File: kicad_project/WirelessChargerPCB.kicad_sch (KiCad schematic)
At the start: 26 parts, among them J1 Screw_Terminal_01x02, J2 Screw_Terminal_01x02, Q1 BD139, Q2 IRFZ44NS, U1 NE555D

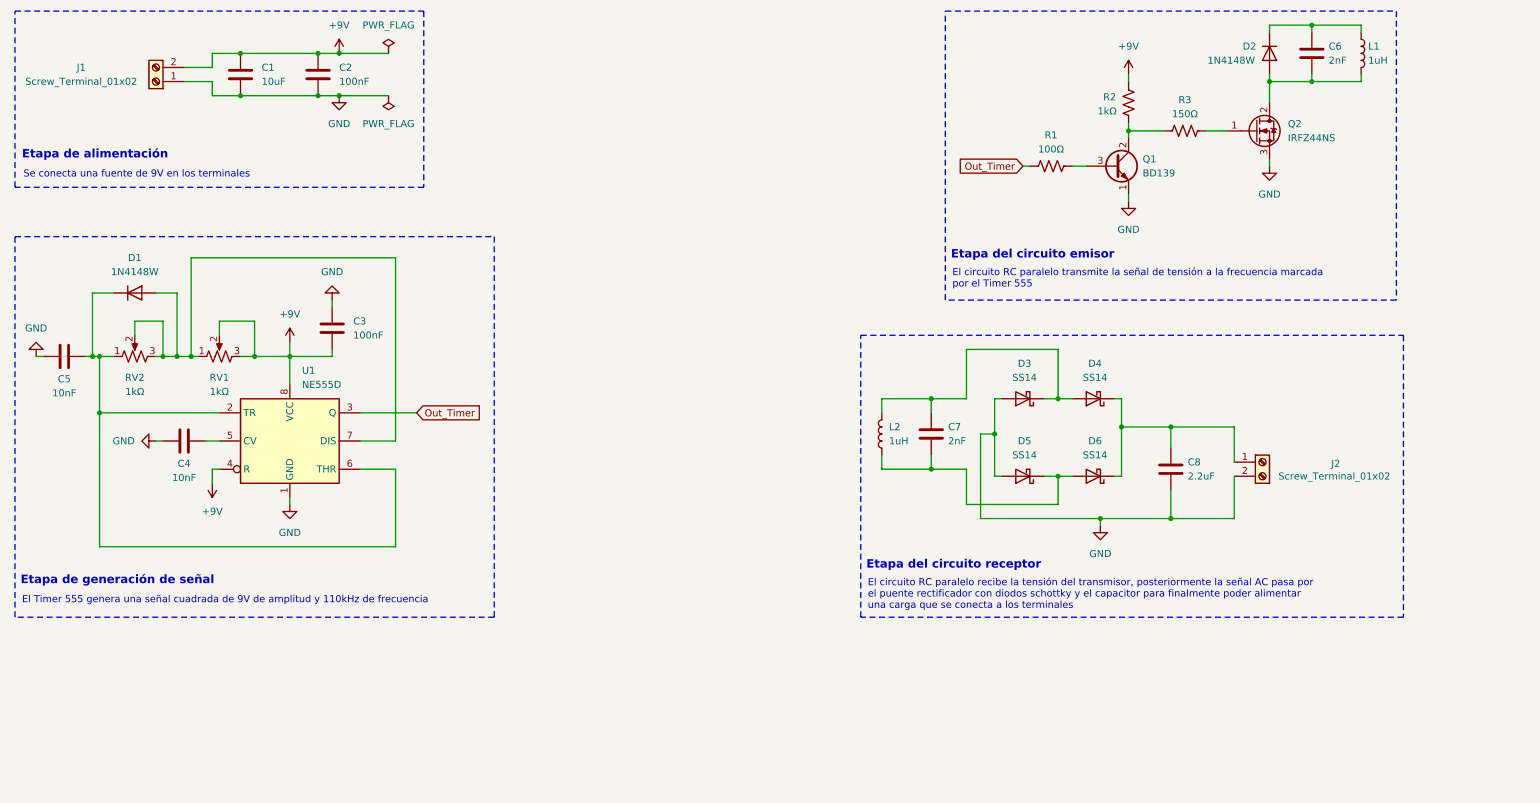
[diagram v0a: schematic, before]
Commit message: Agregando huellas y modelos 3D, además de otros cambios en el editor de placas y esquemático
Signed-off-by: ant0305 <anthonycalvo50@gmail.com>
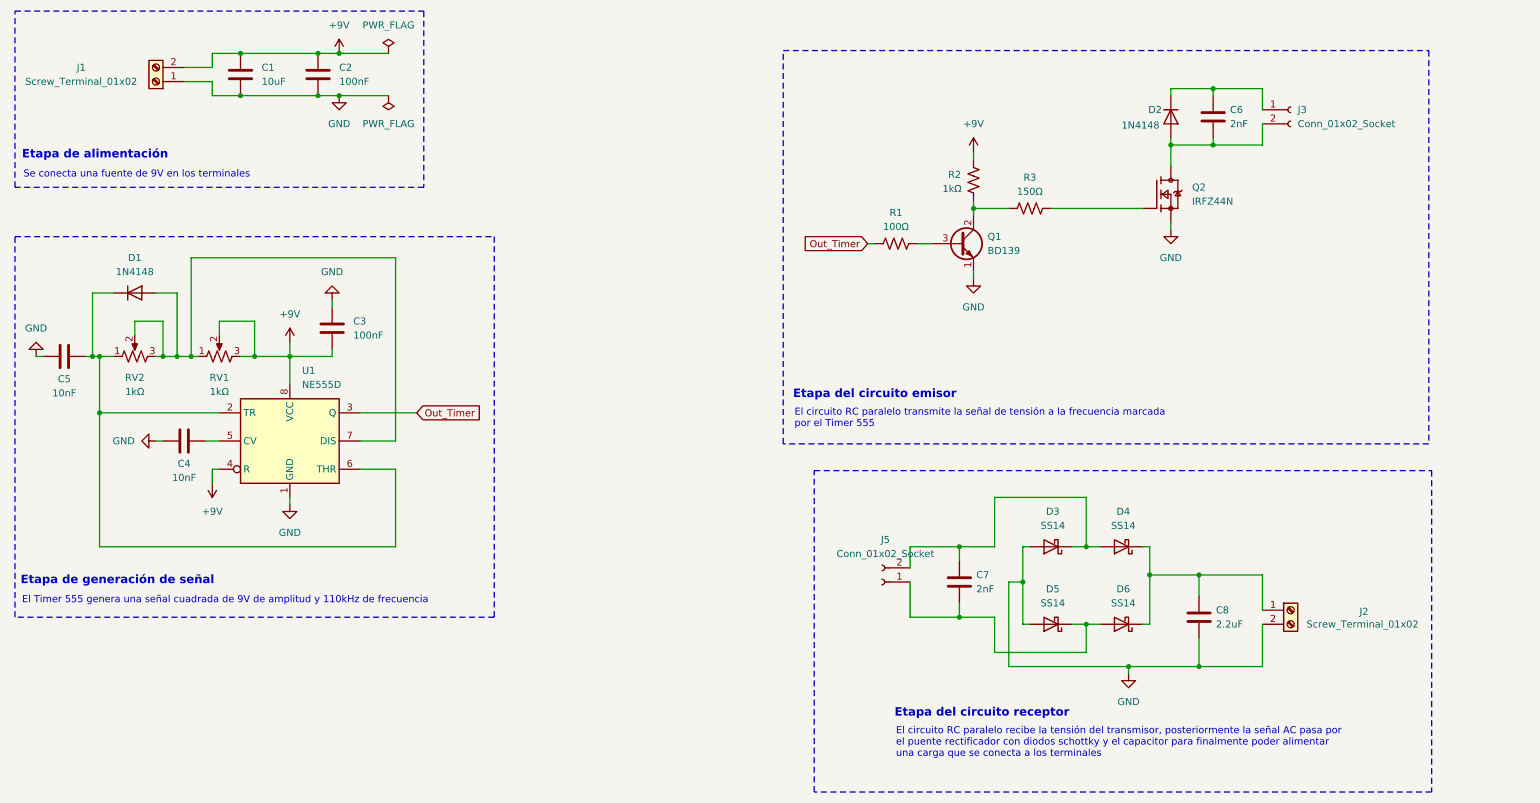
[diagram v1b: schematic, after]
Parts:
- removed D1, D2: 1N4148W, Diode_SMD:D_SOD-123, symbol Diode:1N4148W
- removed L1, L2: 1uH, symbol Device:L
- removed Q2: IRFZ44NS, Package_TO_SOT_SMD:TO-263-2, symbol Device:Q_NMOS_GDS
- added D1, D2: 1N4148, Diode_THT:D_DO-35_SOD27_P7.62mm_Horizontal, symbol Diode:1N4148
- added J3, J5: Conn_01x02_Socket, Connector_PinSocket_2.54mm:PinSocket_1x02_P2.54mm_Vertical, symbol Connector:Conn_01x02_Socket
- added Q2: IRFZ44N, Huellas:TO254P1016X419X2286-3, symbol IRFZ44N:IRFZ44N
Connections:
- net GND: now also Q2.3
- net at RV1.1, RV2.2, RV2.3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: now also D1.2 (A)
- net at C6.1: now also D2.1 (K), J3.1 (Pin_1)
- net at C6.2: now also D2.2 (A), J3.2 (Pin_2), Q2.2
- net at R3.2: now also Q2.1
- net at C5.2, RV2.1, U1.2 (TR)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: now also D1.1 (K)
- net at C7.1, D3.1 (K), D4.2 (A): now also J5.2 (Pin_2)
- net at C7.2, D5.1 (K), D6.2 (A): now also J5.1 (Pin_1)
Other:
- moved on the sheet: C6, C7, C8, D3, D4, D5, D6, J2, Q1, R1, R2, R3

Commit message: Agregando huellas de Heatsinks y relizando acomodo de ambas PCBs
Signed-off-by: RoMadrigal <rmadrigalmontes@gmail.com>
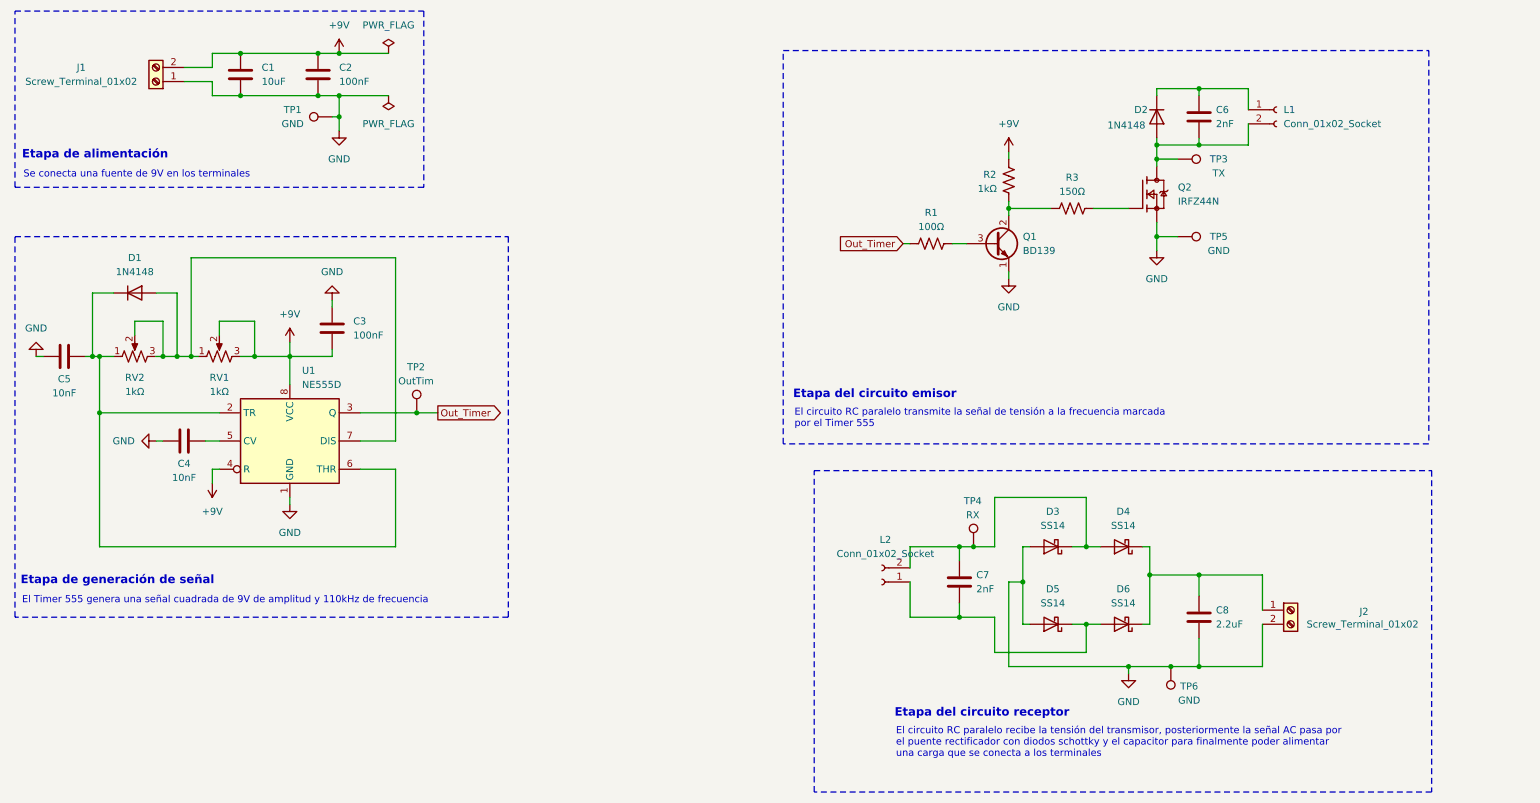
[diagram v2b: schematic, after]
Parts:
- added TP1, TP5, TP6: GND, Connector_PinHeader_2.54mm:PinHeader_1x01_P2.54mm_Vertical, symbol Connector:TestPoint
- added TP2: OutTim, Connector_PinHeader_2.54mm:PinHeader_1x01_P2.54mm_Vertical, symbol Connector:TestPoint
- added TP3: TX, Connector_PinHeader_2.54mm:PinHeader_1x01_P2.54mm_Vertical, symbol Connector:TestPoint
- added TP4: RX, Connector_PinHeader_2.54mm:PinHeader_1x01_P2.54mm_Vertical, symbol Connector:TestPoint
- renumbered J3 to L1, J5 to L2
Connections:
- net GND: now also TP1.1, TP5.1, TP6.1
- net Out_Timer: now also TP2.1
- net at C6.2, D2.2 (A), L1.2 (Pin_2)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: now also TP3.1
- net at C7.1, D3.1 (K), D4.2 (A)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: now also TP4.1
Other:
- moved on the sheet: C6, D2, L1, Q1, Q2, R1, R2, R3

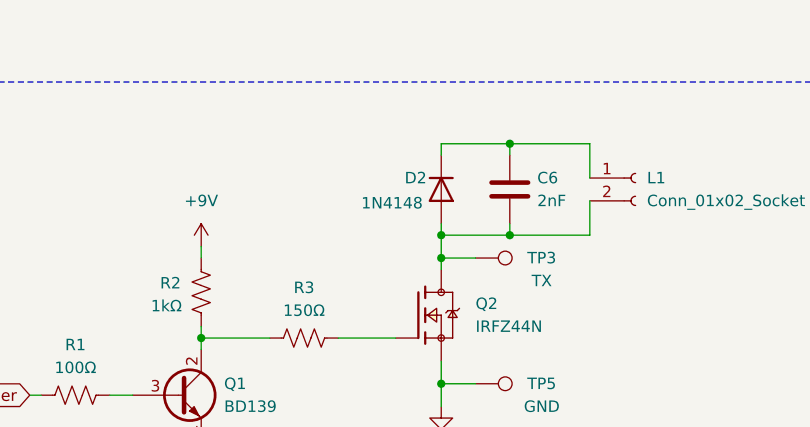
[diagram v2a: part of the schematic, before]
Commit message: Agregando una conexion faltante en el esquematico y actualizando el editor de placas
Signed-off-by: ant0305 <anthonycalvo50@gmail.com>
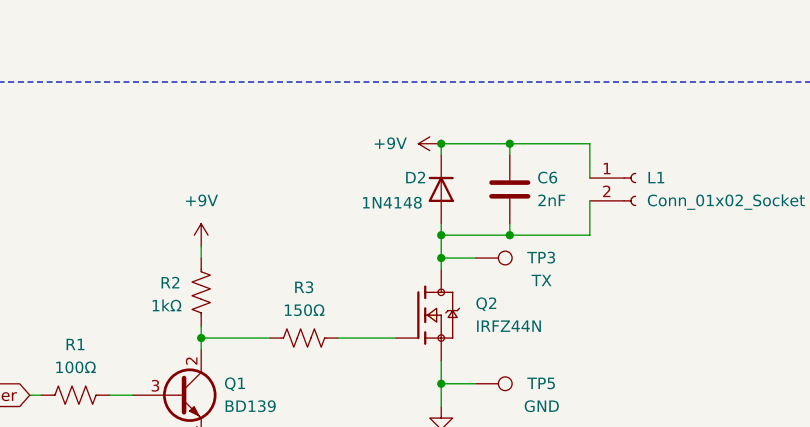
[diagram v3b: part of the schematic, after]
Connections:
- net +9V: now also C6.1, D2.1 (K), L1.1 (Pin_1)
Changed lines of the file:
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@@
+	)
+	(junction
+		(at 231.14 35.56)
+		(diameter 0)
+		(color 0 0 0 0)
 	)
 	(junction
@@
 					(unit 1)
 				)
+			)
+		)
+	)
+	(symbol
+		(lib_id "power:+9V")
+		(at 231.14 35.56 90)
+		(unit 1)
+		(exclude_from_sim no)
+		(in_bom yes)
+		(on_board yes)
+		(dnp no)
+		(fields_autoplaced yes)
+		(property "Reference" "#PWR013"
+			(at 234.95 35.56 0)
+			(effects
+				(font
+					(size 1.27 1.27)
+				)
+				(hide yes)
+			)
+		)
+		(property "Value" "+9V"
+			(at 227.33 35.5599 90)
+			(effects
+				(font
+					(size 1.27 1.27)
+				)
+				(justify left)
+			)
+		)
+		(property "Footprint" ""
+			(at 231.14 35.56 0)
+			(effects
+				(font
+					(size 1.27 1.27)
+				)
+				(hide yes)
+			)
+		)
+		(property "Datasheet" ""
+			(at 231.14 35.56 0)
+			(effects
+				(font
+					(size 1.27 1.27)
+				)
+				(hide yes)
+			)
+		)
+		(property "Description" "Power symbol creates a global label with name \"+9V\""
+			(at 231.14 35.56 0)
+			(effects
+				(font
+					(size 1.27 1.27)
+				)
+				(hide yes)
+			)
+		)
+		(pin "1"
+		)
+		(instances
+			(project "WirelessChargerPCB"
+				(path "/b69418bb-1d9c-4542-932d-c618456e07de"
+					(reference "#PWR013")
+					(unit 1)
+				)

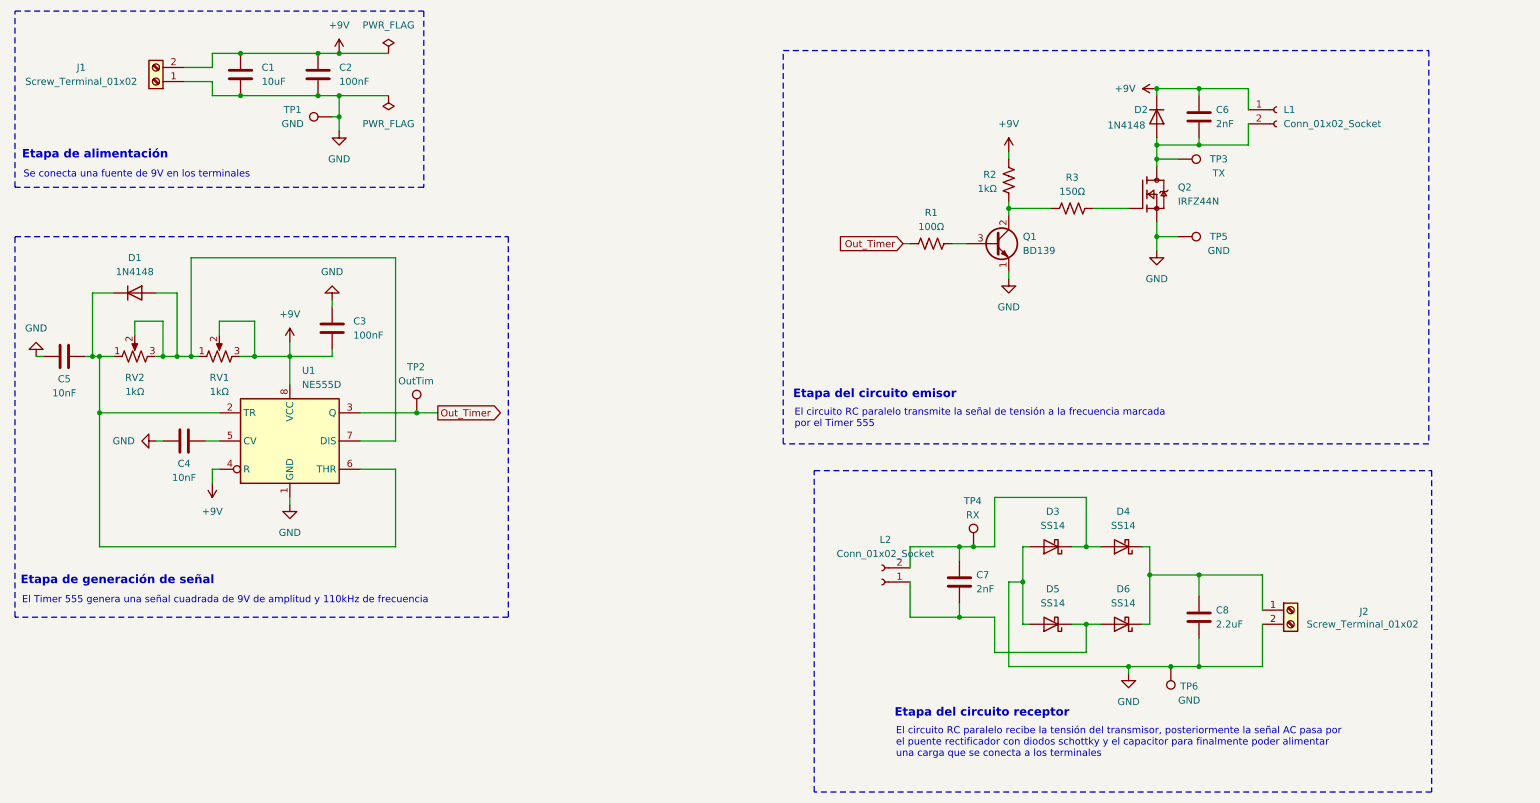
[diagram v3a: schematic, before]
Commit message: Agregando nuevos puntos de prueba y corrigiendo +9V faltante
Signed-off-by: RoMadrigal <rmadrigalmontes@gmail.com>
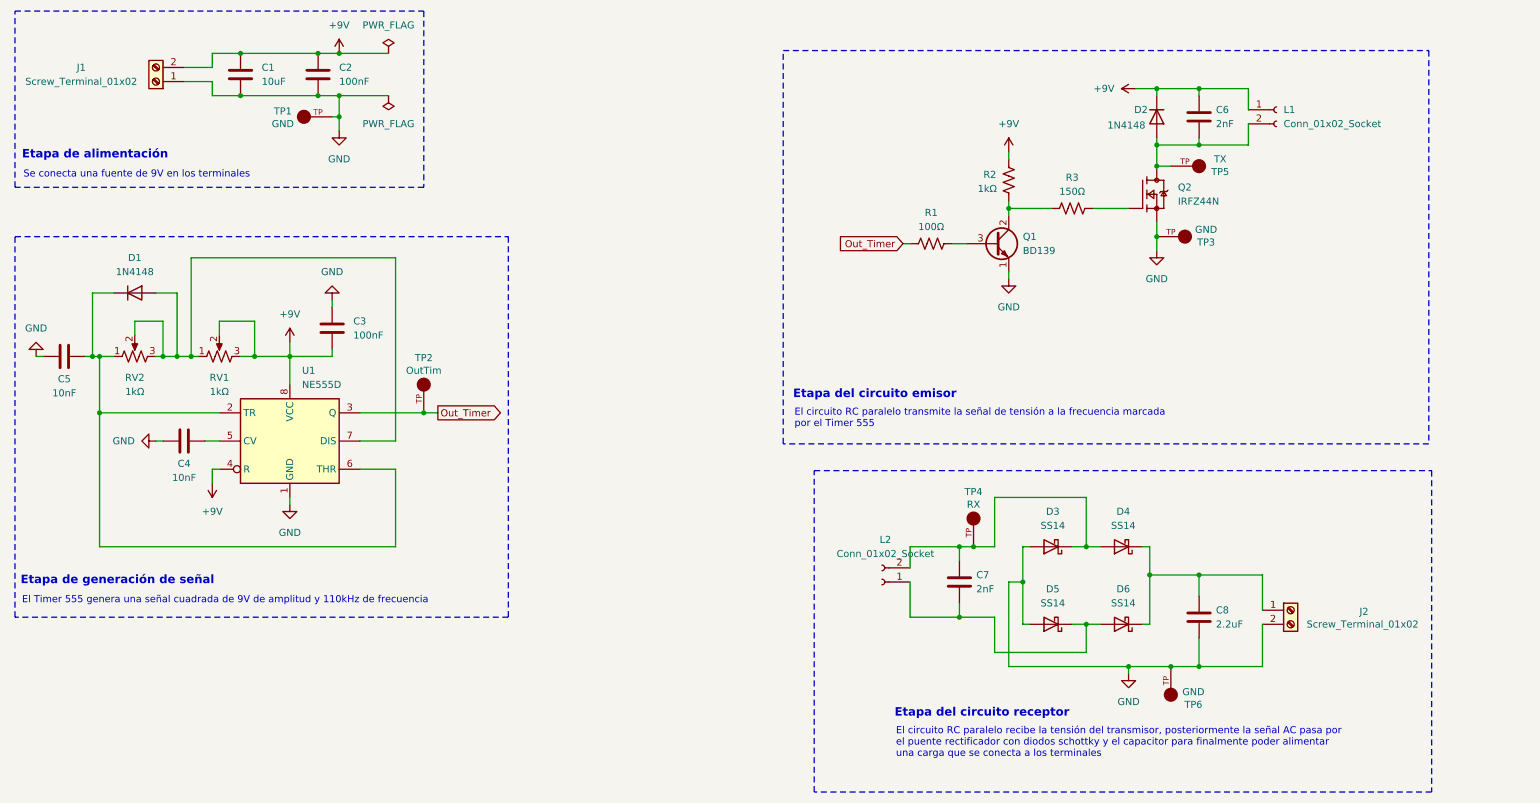
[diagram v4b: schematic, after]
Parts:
- removed TP1, TP5, TP6: GND, Connector_PinHeader_2.54mm:PinHeader_1x01_P2.54mm_Vertical, symbol Connector:TestPoint
- removed TP2: OutTim, Connector_PinHeader_2.54mm:PinHeader_1x01_P2.54mm_Vertical, symbol Connector:TestPoint
- removed TP3: TX, Connector_PinHeader_2.54mm:PinHeader_1x01_P2.54mm_Vertical, symbol Connector:TestPoint
- removed TP4: RX, Connector_PinHeader_2.54mm:PinHeader_1x01_P2.54mm_Vertical, symbol Connector:TestPoint
- added TP1, TP3, TP6: GND, TestPoint:KEYSTONE_5263, symbol TestPoint:5263
- added TP2: OutTim, TestPoint:KEYSTONE_5263, symbol TestPoint:5263
- added TP4: RX, TestPoint:KEYSTONE_5263, symbol TestPoint:5263
- added TP5: TX, TestPoint:KEYSTONE_5263, symbol TestPoint:5263
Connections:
- net GND: now also TP1.TP, TP3.TP, TP6.TP
- net Out_Timer: now also TP2.TP
- net at C6.2, D2.2 (A), L1.2 (Pin_2)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: now also TP5.TP
- net at C7.1, D3.1 (K), D4.2 (A)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: now also TP4.TP
